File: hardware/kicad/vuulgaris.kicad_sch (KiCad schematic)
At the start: 264 parts, among them J1 TFPUSH, J10 PJ-603_C41409498, J11 TYPE-C-31-M-12, J12 FACEPLATE 2x5 IDC, J2 PJ-376, J3 PJ-376, J4 PJ-376, J5 PJ-376, J7 PJ-603_C41409498, J8 PJ-603_C41409498, J9 PJ-603_C41409498, Q1 J113 / MMBFJ113, Q2 J113 / MMBFJ113, SW1 SW_DPDT_FLAT, SW2 SW_DPDT_FLAT, SW4 12x12 tactile, SW5 12x12 tactile, SW6 12x12 tactile, SW7 12x12 tactile, SW8 12x12 tactile, SW9 12x12 tactile, U1 ES_DAISY_PATCH_SM_REV1, U101 V3205SD, U102 TL072_FLAT, U103 TL072_FLAT, U104 CD4046B, U106 TL072_FLAT, U201 V3205SD, U202 TL072_FLAT, U203 TL072_FLAT, U204 CD4046B, U206 TL072_FLAT, U3 MCP23017-E_SO, U301 TL084, U302 TL074, U4 MCP23017-E_SO, U401 TL084, U402 TL074, U5 AMS1117-3.3, U6 AMS1117-3.3, U7 DKM10E-12, U8 78L05

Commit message: hardware: buttons become TS1103S-12X12X14DIP, plunger through a 6.6mm hole
The old part could never have worked and the panel hole was wrong with it.

TC-1212-7.3-160G is 7.3mm tall against a faceplate outer face at 11.6mm, so it
did not reach the panel at all. There is no 16mm part in that family at LCSC --
it stops at 12.0H, which would still have stood only 0.4mm proud. And the 4.5mm
panel hole was sized for a 4mm stem, but the HCTL part's stem is 3.8mm SQUARE,
a 5.37mm diagonal that would never have passed it at any height.

TS1103S-12X12X14DIP (CAX, LCSC C54573007) is 14.0mm -> 2.4mm proud, with a 6.2mm
round plunger through a hole widened to 6.6mm. Its PCB pattern is 4 x 1.2mm at
12.5 x 5.0, which is what KEY-TH_4P-L12.0-W12.0-P5.00-LS12.5 already is, so the
footprint, netlist and button placement are untouched. Part-number swap only.

The snap-on cap is gone -- it existed only because the switch could not reach the
panel. ENC0 moves 2.7mm as the control column re-centres on a 6.6mm hole instead
of a 12mm cap.

Three new generator checks, one per thing that was wrong: proud height against
the 11.6mm outer face, plunger against its hole, and body-to-body row clearance.
40 checks pass. 849/849 connections verified, 0 unintended, no pad overlaps.
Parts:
- removed SW4, SW5, SW6, SW7, SW8, SW9: 12x12 tactile, vuulgaris:KEY-TH_4P-L12.0-W12.0-P5.00-LS12.5, symbol vuulgaris:TC-1212-7.3-160G
- added SW4, SW5, SW6, SW7, SW8, SW9: 12x12 tactile, vuulgaris:KEY-TH_4P-L12.0-W12.0-P5.00-LS12.5, symbol vuulgaris:TS1103S-12X12X14DIP
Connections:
- net BTN1: now also SW4.1, SW4.3
- net BTN2: now also SW5.1, SW5.3
- net BTN3: now also SW6.1, SW6.3
- net BTN4: now also SW7.1, SW7.3
- net BTN5: now also SW8.1, SW8.3
- net BTN6: now also SW9.1, SW9.3
- net GND: now also SW4.2, SW4.4, SW5.2, SW5.4, SW6.2, SW6.4, SW7.2, SW7.4, SW8.2, SW8.4, SW9.2, SW9.4
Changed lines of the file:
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@@
     (pin "6")
   )
-  (symbol (lib_id "vuulgaris:TC-1212-7.3-160G") (at 70 430 0) (unit 1)
+  (symbol (lib_id "vuulgaris:TS1103S-12X12X14DIP") (at 70 430 0) (unit 1)
     (in_bom yes) (on_board yes) (dnp no)
     (property "Reference" "SW4" (at 70 418 0) (effects (font (size 1.27 1.27))))
@@
     (pin "1")
   )
-  (symbol (lib_id "vuulgaris:TC-1212-7.3-160G") (at 150 430 0) (unit 1)
+  (symbol (lib_id "vuulgaris:TS1103S-12X12X14DIP") (at 150 430 0) (unit 1)
     (in_bom yes) (on_board yes) (dnp no)
     (property "Reference" "SW5" (at 150 418 0) (effects (font (size 1.27 1.27))))
@@
     (pin "1")
   )
-  (symbol (lib_id "vuulgaris:TC-1212-7.3-160G") (at 70 490 0) (unit 1)
+  (symbol (lib_id "vuulgaris:TS1103S-12X12X14DIP") (at 70 490 0) (unit 1)
     (in_bom yes) (on_board yes) (dnp no)
     (property "Reference" "SW6" (at 70 478 0) (effects (font (size 1.27 1.27))))
@@
     (pin "1")
   )
-  (symbol (lib_id "vuulgaris:TC-1212-7.3-160G") (at 150 490 0) (unit 1)
+  (symbol (lib_id "vuulgaris:TS1103S-12X12X14DIP") (at 150 490 0) (unit 1)
     (in_bom yes) (on_board yes) (dnp no)
     (property "Reference" "SW7" (at 150 478 0) (effects (font (size 1.27 1.27))))
@@
     (pin "1")
   )
-  (symbol (lib_id "vuulgaris:TC-1212-7.3-160G") (at 230 430 0) (unit 1)
+  (symbol (lib_id "vuulgaris:TS1103S-12X12X14DIP") (at 230 430 0) (unit 1)
     (in_bom yes) (on_board yes) (dnp no)
     (property "Reference" "SW8" (at 230 418 0) (effects (font (size 1.27 1.27))))
@@
     (pin "1")
   )
-  (symbol (lib_id "vuulgaris:TC-1212-7.3-160G") (at 230 490 0) (unit 1)
+  (symbol (lib_id "vuulgaris:TS1103S-12X12X14DIP") (at 230 490 0) (unit 1)
     (in_bom yes) (on_board yes) (dnp no)
     (property "Reference" "SW9" (at 230 478 0) (effects (font (size 1.27 1.27))))

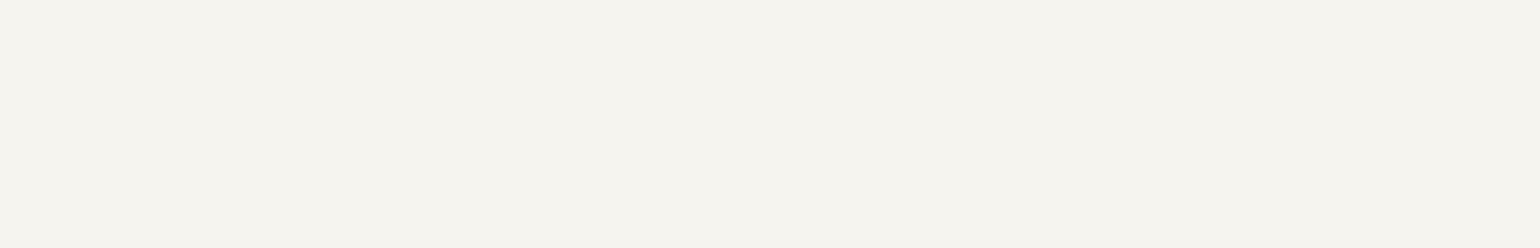
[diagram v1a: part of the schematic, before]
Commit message: hardware: through-hole power test points, TP1-TP5
+12V, -12V, +5V, +5V BBD and GND in the top-left corner at 4.5mm pitch. New
footprint TestPoint_TH_D1.0mm, 1.0mm drill / 2.0mm pad.

Two 5V points rather than one: P5V is the Daisy's, feeding the OLED and MSP430
regulators; P5V_BBD is the AMS1117 output, and that is the rail whose current
could not be budgeted because Panasonic never specced an I_DD for the MN3205.

The silk shows the VALUE, not the reference -- TP3 tells you nothing at a bench.
Through-hole so they can be probed from either face, since the front sits under
the faceplate. Placed at the far end from the power stage deliberately: bring-up
wants to know what the far end receives, not what the regulator makes. GND sits
in the row so probe loops stay short.

854/854 verified, 0 unintended, no pad overlaps.
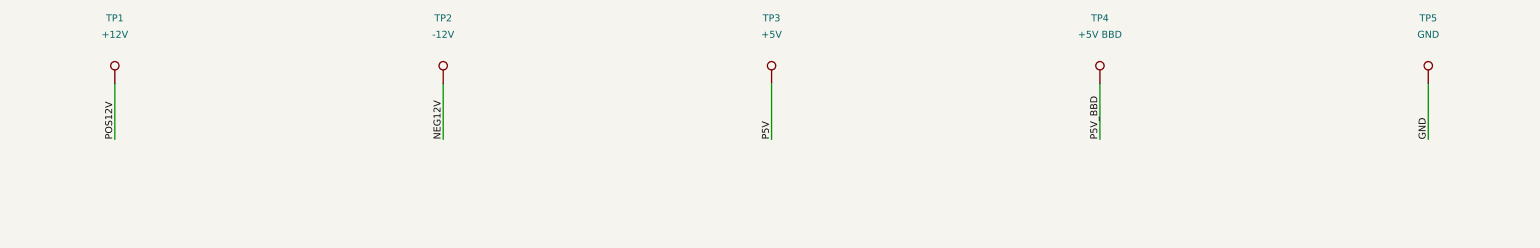
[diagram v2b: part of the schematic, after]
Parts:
- added TP1: +12V, vuulgaris:TestPoint_TH_D1.0mm, symbol vuulgaris:TestPoint
- added TP2: -12V, vuulgaris:TestPoint_TH_D1.0mm, symbol vuulgaris:TestPoint
- added TP3: +5V, vuulgaris:TestPoint_TH_D1.0mm, symbol vuulgaris:TestPoint
- added TP4: +5V BBD, vuulgaris:TestPoint_TH_D1.0mm, symbol vuulgaris:TestPoint
- added TP5: GND, vuulgaris:TestPoint_TH_D1.0mm, symbol vuulgaris:TestPoint
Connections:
- net GND: now also TP5.1
- net NEG12V: now also TP2.1
- net P5V: now also TP3.1
- net P5V_BBD: now also TP4.1
- net POS12V: now also TP1.1
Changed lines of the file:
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@@
     (pin "1")
   )
+  (symbol (lib_id "vuulgaris:TestPoint") (at 860 60 0) (unit 1)
+    (in_bom yes) (on_board yes) (dnp no)
+    (property "Reference" "TP1" (at 860 48 0) (effects (font (size 1.27 1.27))))
+    (property "Value" "+12V" (at 860 51 0) (effects (font (size 1.27 1.27))))
+    (property "Footprint" "vuulgaris:TestPoint_TH_D1.0mm" (at 860 60 0) (effects (font (size 1.27 1.27)) hide))
+    (property "Datasheet" "" (at 860 60 0) (effects (font (size 1.27 1.27)) hide))
+    (pin "1")
+  )
+  (symbol (lib_id "vuulgaris:TestPoint") (at 920 60 0) (unit 1)
+    (in_bom yes) (on_board yes) (dnp no)
+    (property "Reference" "TP2" (at 920 48 0) (effects (font (size 1.27 1.27))))
+    (property "Value" "-12V" (at 920 51 0) (effects (font (size 1.27 1.27))))
+    (property "Footprint" "vuulgaris:TestPoint_TH_D1.0mm" (at 920 60 0) (effects (font (size 1.27 1.27)) hide))
+    (property "Datasheet" "" (at 920 60 0) (effects (font (size 1.27 1.27)) hide))
+    (pin "1")
+  )
+  (symbol (lib_id "vuulgaris:TestPoint") (at 980 60 0) (unit 1)
+    (in_bom yes) (on_board yes) (dnp no)
+    (property "Reference" "TP3" (at 980 48 0) (effects (font (size 1.27 1.27))))
+    (property "Value" "+5V" (at 980 51 0) (effects (font (size 1.27 1.27))))
+    (property "Footprint" "vuulgaris:TestPoint_TH_D1.0mm" (at 980 60 0) (effects (font (size 1.27 1.27)) hide))
+    (property "Datasheet" "" (at 980 60 0) (effects (font (size 1.27 1.27)) hide))
+    (pin "1")
+  )
+  (symbol (lib_id "vuulgaris:TestPoint") (at 1040 60 0) (unit 1)
+    (in_bom yes) (on_board yes) (dnp no)
+    (property "Reference" "TP4" (at 1040 48 0) (effects (font (size 1.27 1.27))))
+    (property "Value" "+5V BBD" (at 1040 51 0) (effects (font (size 1.27 1.27))))
+    (property "Footprint" "vuulgaris:TestPoint_TH_D1.0mm" (at 1040 60 0) (effects (font (size 1.27 1.27)) hide))
+    (property "Datasheet" "" (at 1040 60 0) (effects (font (size 1.27 1.27)) hide))
+    (pin "1")
+  )
+  (symbol (lib_id "vuulgaris:TestPoint") (at 1100 60 0) (unit 1)
+    (in_bom yes) (on_board yes) (dnp no)
+    (property "Reference" "TP5" (at 1100 48 0) (effects (font (size 1.27 1.27))))
+    (property "Value" "GND" (at 1100 51 0) (effects (font (size 1.27 1.27))))
+    (property "Footprint" "vuulgaris:TestPoint_TH_D1.0mm" (at 1100 60 0) (effects (font (size 1.27 1.27)) hide))
+    (property "Datasheet" "" (at 1100 60 0) (effects (font (size 1.27 1.27)) hide))
+    (pin "1")
+  )
   (symbol (lib_id "vuulgaris:ES_DAISY_PATCH_SM_REV1") (at 150 170 0) (unit 1)
     (in_bom yes) (on_board yes) (dnp no)
@@
   (wire (pts (xy 224.92 493.81) (xy 214.76 493.81)) (stroke (width 0) (type solid)))
   (wire (pts (xy 235.08 493.81) (xy 245.24 493.81)) (stroke (width 0) (type solid)))
+  (wire (pts (xy 860.0 60.0) (xy 860.0 70.16)) (stroke (width 0) (type solid)))
+  (wire (pts (xy 920.0 60.0) (xy 920.0 70.16)) (stroke (width 0) (type solid)))
+  (wire (pts (xy 980.0 60.0) (xy 980.0 70.16)) (stroke (width 0) (type solid)))
+  (wire (pts (xy 1040.0 60.0) (xy 1040.0 70.16)) (stroke (width 0) (type solid)))
+  (wire (pts (xy 1100.0 60.0) (xy 1100.0 70.16)) (stroke (width 0) (type solid)))
   (wire (pts (xy 148.73 205.56) (xy 148.73 215.72)) (stroke (width 0) (type solid)))
   (wire (pts (xy 127.14 185.24) (xy 116.98 185.24)) (stroke (width 0) (type solid)))
@@
     (effects (font (size 1.27 1.27)) (justify left bottom))
   )
+  (label "POS12V" (at 860.0 70.16 270) (fields_autoplaced)
+    (effects (font (size 1.27 1.27)) (justify left bottom))
+  )
+  (label "NEG12V" (at 920.0 70.16 270) (fields_autoplaced)
+    (effects (font (size 1.27 1.27)) (justify left bottom))
+  )
+  (label "P5V" (at 980.0 70.16 270) (fields_autoplaced)
+    (effects (font (size 1.27 1.27)) (justify left bottom))
+  )
+  (label "P5V_BBD" (at 1040.0 70.16 270) (fields_autoplaced)
+    (effects (font (size 1.27 1.27)) (justify left bottom))
+  )
+  (label "GND" (at 1100.0 70.16 270) (fields_autoplaced)
+    (effects (font (size 1.27 1.27)) (justify left bottom))
+  )
